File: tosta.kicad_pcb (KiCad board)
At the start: 2 copper layers, 73.7 x 50.8 mm, 29 parts, among them J1 UEXT, Q1 MMBT3904, SW1 SW_Push, SW2 SW_Push, SW3 SW_Push, SW4 SW_Push, U1 STM32G030KxT, U2 LPH7366

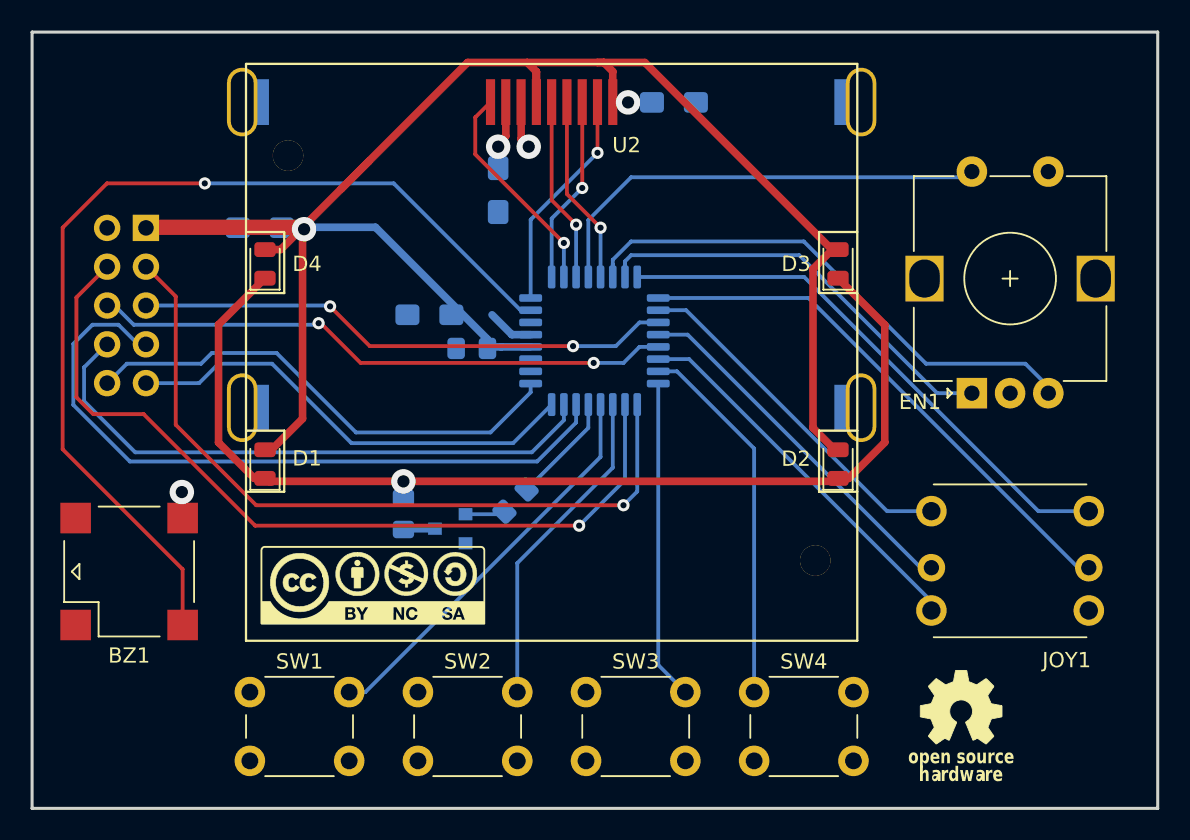
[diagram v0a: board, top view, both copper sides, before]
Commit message: Added SWD header
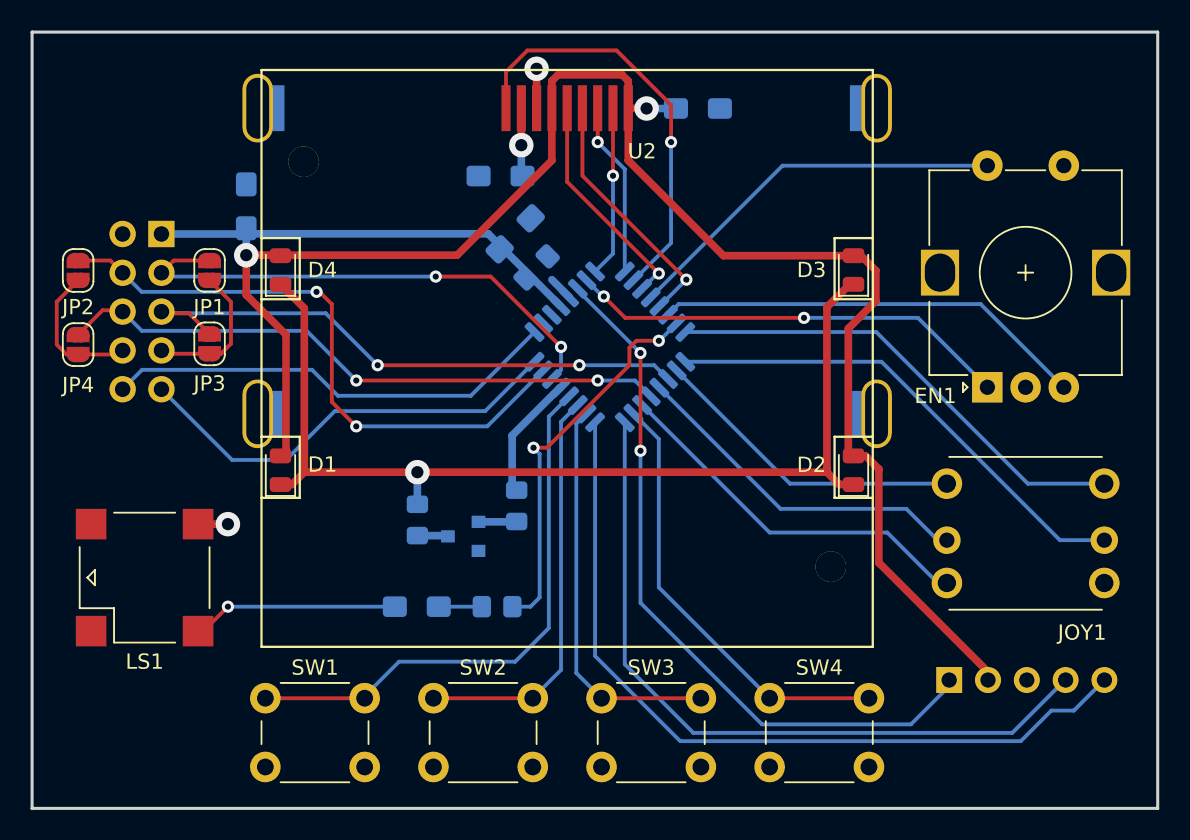
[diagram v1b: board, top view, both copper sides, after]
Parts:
- added C6: 4.7u, Capacitor_Tantalum_SMD:CP_EIA-3216-12_Kemet-S_Pad1.58x1.35mm_HandSolder, B.Cu at (72.6, 85.1)
- added J2: SWD, Connector_PinHeader_2.54mm:PinHeader_1x05_P2.54mm_Vertical, B.Cu at (107.5, 89.9)
- added JP1: SolderJumper_2_Open, Jumper:SolderJumper-2_P1.3mm_Open_RoundedPad1.0x1.5mm, F.Cu at (59.1, 63.1)
- added JP2: SolderJumper_2_Open, Jumper:SolderJumper-2_P1.3mm_Open_RoundedPad1.0x1.5mm, F.Cu at (50.5, 63.1)
- added JP3: SolderJumper_2_Open, Jumper:SolderJumper-2_P1.3mm_Open_RoundedPad1.0x1.5mm, F.Cu at (59.1, 67.9)
- added JP4: SolderJumper_2_Open, Jumper:SolderJumper-2_P1.3mm_Open_RoundedPad1.0x1.5mm, F.Cu at (50.5, 67.9)
- added R3: 220, Resistor_SMD:R_0805_2012Metric_Pad1.20x1.40mm_HandSolder, B.Cu at (77.9, 85.1)
- CC_BYNCSA, OSHW: moved to B.Cu
- H1, H2, H3, H4: value MountingHole_Pad -> MountingHole
- LS1: renamed from BZ1; value Buzzer -> 16ohm
- moved OSHW 44.0 mm to (66.1, 80.5), turned to 180 degrees
- moved svg2mod 36.8 mm to (89.9, 79.7), turned to 180 degrees
- moved CC_BYNCSA 16.1 mm to (53.7, 84.5), turned to -90 degrees
- moved C2 7.72 mm to (79.1, 60.7), turned to 45 degrees
- moved C3 6.79 mm to (80.5, 62.9), turned to 45 degrees
- moved JOY1 2.07 mm to (112.5, 80.3)
- moved C1 1.66 mm to (61.5, 58.9), turned to 90 degrees
- moved C5 1.62 mm to (91.0, 52.5)
- moved U2 1.09 mm to (82.5, 49.9)
- moved SW2 1.09 mm to (73.7, 91.0)
- moved SW3 1.09 mm to (84.7, 91.0)
- moved SW4 1.09 mm to (95.7, 91.0)
- moved U1 1.09 mm to (85.3, 68.1), turned to -45 degrees
- moved D3 1.09 mm to (101.2, 63.0)
- moved D4 1.09 mm to (63.7, 63.0)
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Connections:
- net SCK renamed SCK2
- net SCL renamed SCL/MISO2
- net SDA renamed SDA/MOSI2
- net ~SSEL renamed ~nSSEL2
- J1 pad 3: TXD -> TXD/MISO2
- J1 pad 4: RXD -> RXD/MOSI2
- J1 pad 7: MISO -> Net-(J1-Pad7)
- J1 pad 8: MOSI -> Net-(J1-Pad8)
- LS1 pad 1: Net-(BZ1-Pad1) -> Net-(LS1-Pad1)
- U1 pad 15: EN1A -> Net-(U1-Pad15)
- U1 pad 24: SW3 -> SWDIO
- U1 pad 25: TXD -> SWCLK
- U1 pad 26: RXD -> SW3
- U1 pad 30: MISO -> TXD/MISO2
- U1 pad 31: MOSI -> RXD/MOSI2
- U1 pad 6: Net-(U1-Pad6) -> ~nRST
- U1 pad 7: Net-(BZ1-Pad1) -> EN1A
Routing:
- net Net-(BZ1-Pad1): track 65.0 -> 0.00 mm, vias 1 -> 0
- net RXD: track 55.2 -> 0.00 mm, vias 1 -> 0
- net SWCLK: track 0.00 -> 52.6 mm
- net TXD: track 49.6 -> 0.00 mm, vias 1 -> 0
- net SWDIO: track 0.00 -> 47.9 mm
- net ~nRST: track 0.00 -> 46.7 mm, vias 0 -> 2
- net MISO: track 46.5 -> 0.00 mm
- net RXD/MOSI2: track 0.00 -> 40.2 mm, vias 0 -> 2
- net MOSI: track 39.0 -> 0.00 mm
- net TXD/MISO2: track 0.00 -> 33.6 mm, vias 0 -> 2
- net Net-(U1-Pad15): track 0.00 -> 25.4 mm, vias 0 -> 2
- net LCD_~RST: track 14.3 -> 27.7 mm
- net Net-(LS1-Pad1): track 0.00 -> 13.3 mm, vias 0 -> 1
- net +3V3: track 123.0 -> 135.3 mm
- net SW1: track 26.2 -> 36.1 mm
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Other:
- net class Default removed
- net class Power removed
- board text added: "REV. A"
- board text added: "SWD"
- board text added: "https://git.lattuga.net/asdrea/tosta"
- board text removed: "rev: A"

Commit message: Updated speaker driver
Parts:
- added C7: 68n, Capacitor_SMD:C_0805_2012Metric_Pad1.18x1.45mm_HandSolder, B.Cu at (60.3, 87.9)
- C3: value 100n -> 68n
- moved C4 3.56 mm to (74.7, 55.8)
- moved C3 0.34 mm to (80.7, 62.6)
- renumbered J1 to UEXT
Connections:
- U1 pad 2: Net-(U1-Pad2) -> (no net)
- U1 pad 3: Net-(U1-Pad3) -> (no net)
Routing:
- net Net-(C6-Pad2): track 13.3 -> 15.0 mm
- net Net-(C4-Pad1): track 4.36 -> 5.79 mm
- net GND: track 6.16 -> 7.08 mm
- net LCD_~RST: track 27.7 -> 27.1 mm
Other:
- board text added: "3V3"
- board text added: "GND"
- board text added: "JLCJLCJLCJLC"
- board text added: "SWCLK"
- board text added: "SWDIO"
- board text added: "~RST"
